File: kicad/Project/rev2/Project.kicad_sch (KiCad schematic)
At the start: 56 parts, among them J1 USB_B_Micro, J2 SWD_Connector, J3 Micro_SD_Card_Det1, J4 01x10, J5 02x02, P1 S2B-PH-SM4-TB, Q2 BC817, U5 VEML7700

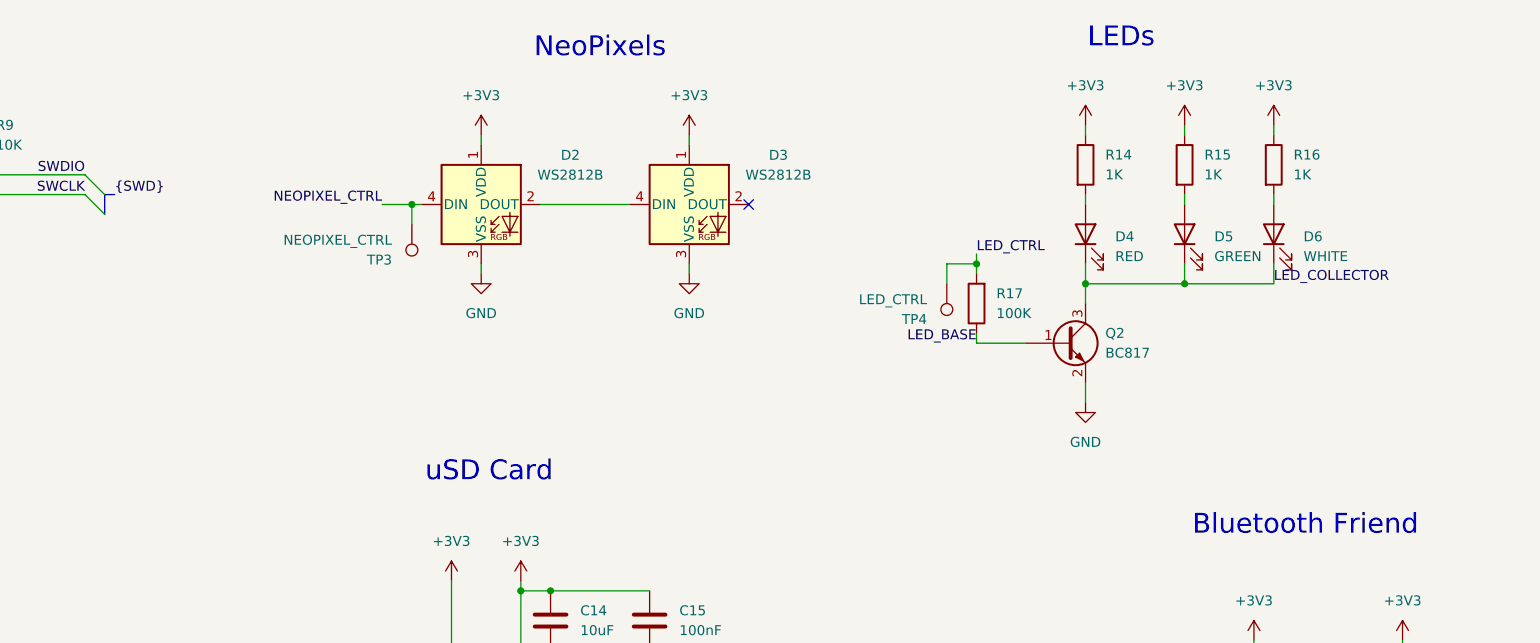
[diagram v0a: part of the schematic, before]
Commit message: Add discovered errata
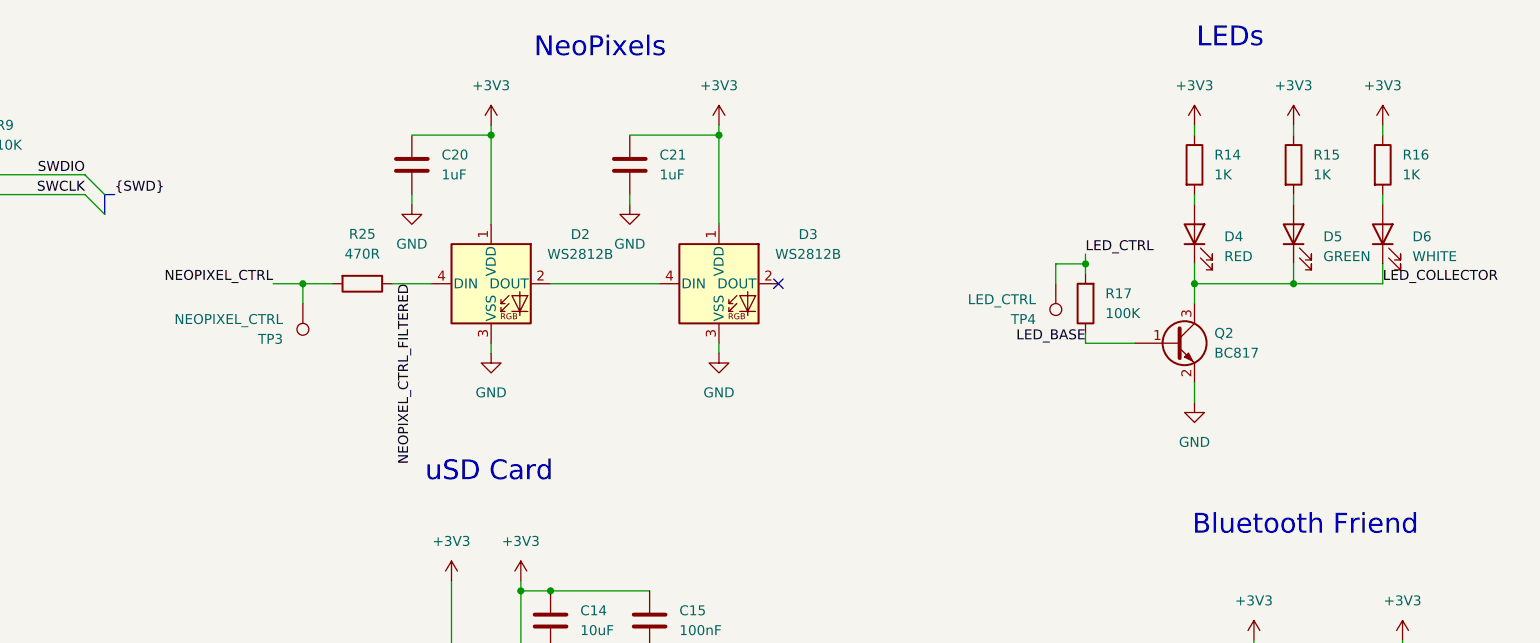
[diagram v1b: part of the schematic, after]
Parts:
- added C20, C21: 1uF, Capacitor_SMD:C_0603_1608Metric_Pad1.08x0.95mm_HandSolder, symbol Device:C
- added R25: 470R, Resistor_SMD:R_0603_1608Metric_Pad0.98x0.95mm_HandSolder, symbol Device:R
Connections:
- net +3V3: now also C20.1, C21.1
- net GND: now also C20.2, C21.2
- net NEOPIXEL_CTRL: now also R25.2; no longer D2.4 (DIN)
- new net NEOPIXEL_CTRL_FILTERED: D2.4 (DIN), R25.1
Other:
- moved on the sheet: D2, D3, D4, D5, D6, Q2, R14, R15, R16, R17, TP3, TP4

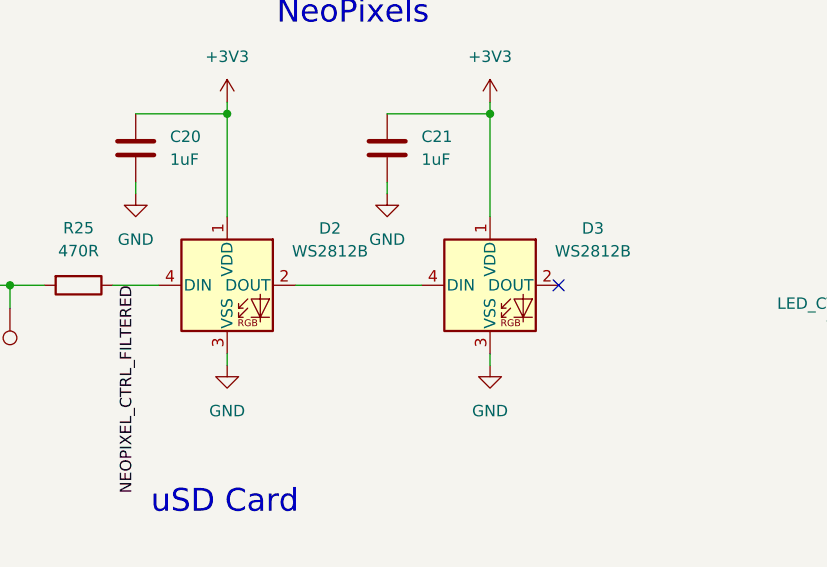
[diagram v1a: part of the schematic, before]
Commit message: Use the more common NeoPixels
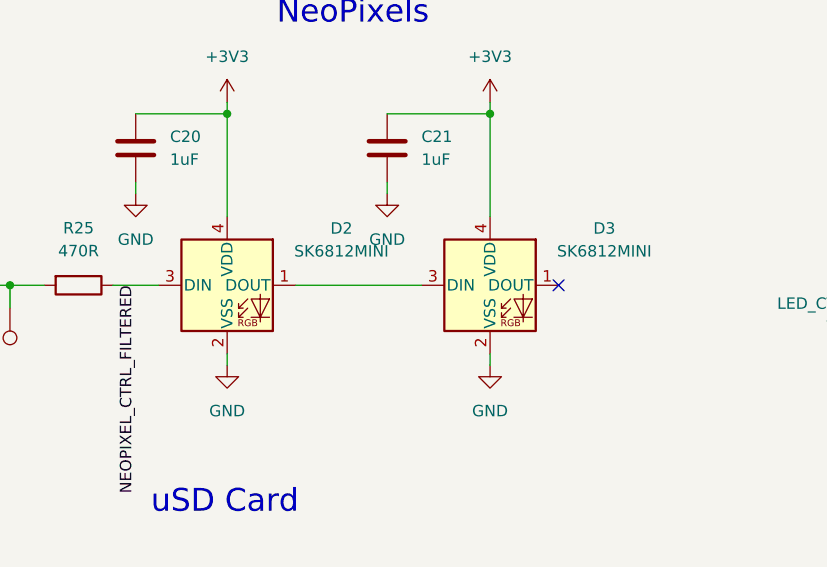
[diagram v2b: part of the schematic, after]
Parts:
- removed D2, D3: WS2812B, LED_SMD:LED_WS2812B_PLCC4_5.0x5.0mm_P3.2mm, symbol LED:WS2812B
- added D2, D3: SK6812MINI, LED_SMD:LED_SK6812MINI_PLCC4_3.5x3.5mm_P1.75mm, symbol LED:SK6812MINI
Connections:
- net +3V3: now also D2.4 (VDD), D3.4 (VDD)
- net GND: now also D2.2 (VSS), D3.2 (VSS)
- net NEOPIXEL_CTRL_FILTERED: now also D2.3 (DIN)
- new net: D2.1 (DOUT), D3.3 (DIN)
